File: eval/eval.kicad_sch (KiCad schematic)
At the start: 10 parts, among them J1 TC2030, U1 STM32G0B1CBTx

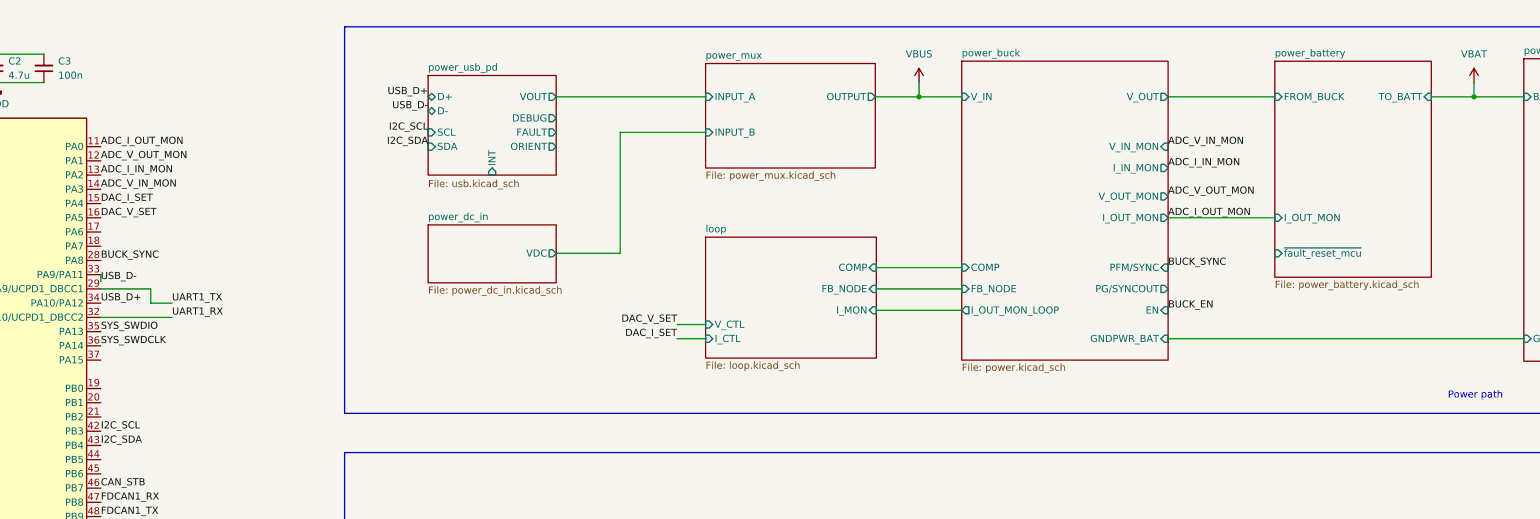
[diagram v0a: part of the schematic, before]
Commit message: [sch] Remote volt-drop detect and NAND latch
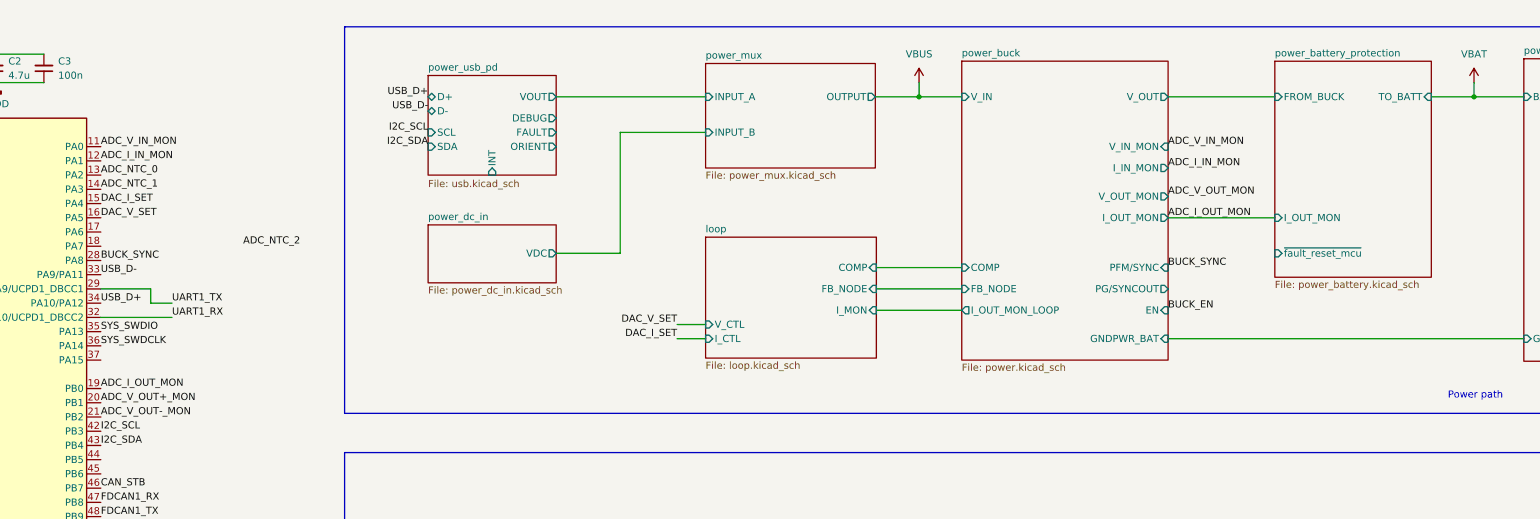
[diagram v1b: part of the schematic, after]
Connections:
- net ADC_I_IN_MON: now also U1.12 (PA1); no longer U1.13 (PA2)
- net ADC_I_OUT_MON: now also U1.19 (PB0); no longer U1.11 (PA0)
- net ADC_V_IN_MON: now also U1.11 (PA0); no longer U1.14 (PA3)
- net ADC_V_OUT_MON: no longer U1.12 (PA1)
- net ADC_V_OUT+_MON: now reaches U1.20 (PB1)
- net ADC_V_OUT-_MON: now reaches U1.21 (PB2)
- new net ADC_NTC_0: U1.13 (PA2)
- new net ADC_NTC_1: U1.14 (PA3)
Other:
- sheet power_battery renamed power_battery_protection
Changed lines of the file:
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@@
 	(wire
 		(pts
-			(xy 107.95 83.82) (xy 107.95 82.55)
-		)
-		(stroke
-			(width 0)
-			(type default)
-		)
-	)
-	(wire
-		(pts
 			(xy 107.95 85.09) (xy 116.84 85.09)
 		)
@@
 	)
 	(label "ADC_I_IN_MON"
+		(at 107.95 62.23 0)
+		(effects
+			(font
+				(size 1.27 1.27)
+			)
+			(justify left bottom)
+		)
+	)
+	(label "ADC_NTC_2"
+		(at 133.35 77.47 0)
+		(effects
+			(font
+				(size 1.27 1.27)
+			)
+			(justify left bottom)
+		)
+	)
+	(label "ADC_I_IN_MON"
 		(at 298.45 63.5 0)
 		(effects
@@
 		)
 	)
-	(label "ADC_I_OUT_MON"
+	(label "ADC_V_IN_MON"
 		(at 107.95 59.69 0)
 		(effects
@@
 		)
 	)
-	(label "ADC_I_IN_MON"
-		(at 107.95 64.77 0)
-		(effects
-			(font
-				(size 1.27 1.27)
-			)
-			(justify left bottom)
-		)
-	)
 	(label "ADC_V_OUT_MON"
 		(at 298.45 68.58 0)
@@
 		)
 	)
+	(label "ADC_I_OUT_MON"
+		(at 107.95 102.87 0)
+		(effects
+			(font
+				(size 1.27 1.27)
+			)
+			(justify left bottom)
+		)
+	)
 	(label "SYS_SWDCLK"
 		(at 63.5 195.58 0)
@@
 		)
 	)
-	(label "ADC_V_OUT_MON"
-		(at 107.95 62.23 0)
+	(label "ADC_V_OUT-_MON"
+		(at 107.95 107.95 0)
+		(effects
+			(font
+				(size 1.27 1.27)
+			)
+			(justify left bottom)
+		)
+	)
+	(label "ADC_NTC_1"
+		(at 107.95 67.31 0)
 		(effects
 			(font
@@
 	)
 	(label "USB_D-"
-		(at 107.95 83.82 0)
+		(at 107.95 82.55 0)
 		(effects
 			(font
@@
 		)
 	)
-	(label "ADC_V_IN_MON"
-		(at 107.95 67.31 0)
+	(label "FDCAN1_RX"
+		(at 107.95 123.19 0)
 		(effects
 			(font
@@
 		)
 	)
-	(label "FDCAN1_RX"
-		(at 107.95 123.19 0)
+	(label "LCD_CS"
+		(at 107.95 133.35 0)
 		(effects
 			(font
@@
 		)
 	)
-	(label "LCD_CS"
-		(at 107.95 133.35 0)
+	(label "ADC_NTC_0"
+		(at 107.95 64.77 0)
 		(effects
 			(font
@@
 		)
 	)
+	(label "ADC_V_OUT+_MON"
+		(at 107.95 105.41 0)
+		(effects
+			(font
+				(size 1.27 1.27)
+			)
+			(justify left bottom)
+		)
+	)
 	(symbol
 		(lib_id "power:GNDA")
@@
 			(color 0 0 0 0)
 		)
-		(property "Sheetname" "power_battery"
+		(property "Sheetname" "power_battery_protection"
 			(at 317.5 43.7384 0)
 			(show_name no)

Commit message: [sch] Use a 74lvc1 as oring of alart
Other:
- sheet power_battery_protection ports: added MCU_EN, NEG_V_ALARM, OVER_I_ALARM; removed ~{fault_reset_mcu}
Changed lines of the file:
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@@
-			)
-		)
-		(pin "~{fault_reset_mcu}" input
-			(at 317.5 78.74 180)
-			(effects
-				(font
-					(size 1.27 1.27)
-				)
-				(justify left)
 			)
 		)
@@
 			(effects
 				(font
+					(size 1.27 1.27)
+				)
+				(justify right)
+			)
+		)
+		(pin "MCU_EN" input
+			(at 345.44 59.69 0)
+			(effects
+				(font
+					(size 1.27 1.27)
+				)
+				(justify right)
+			)
+		)
+		(pin "NEG_V_ALARM" input
+			(at 345.44 63.5 0)
+			(effects
+				(font
+					(size 1.27 1.27)
+				)
+				(justify right)
+			)
+		)
+		(pin "OVER_I_ALARM" input
+			(at 345.44 67.31 0)
+			(effects
+				(font

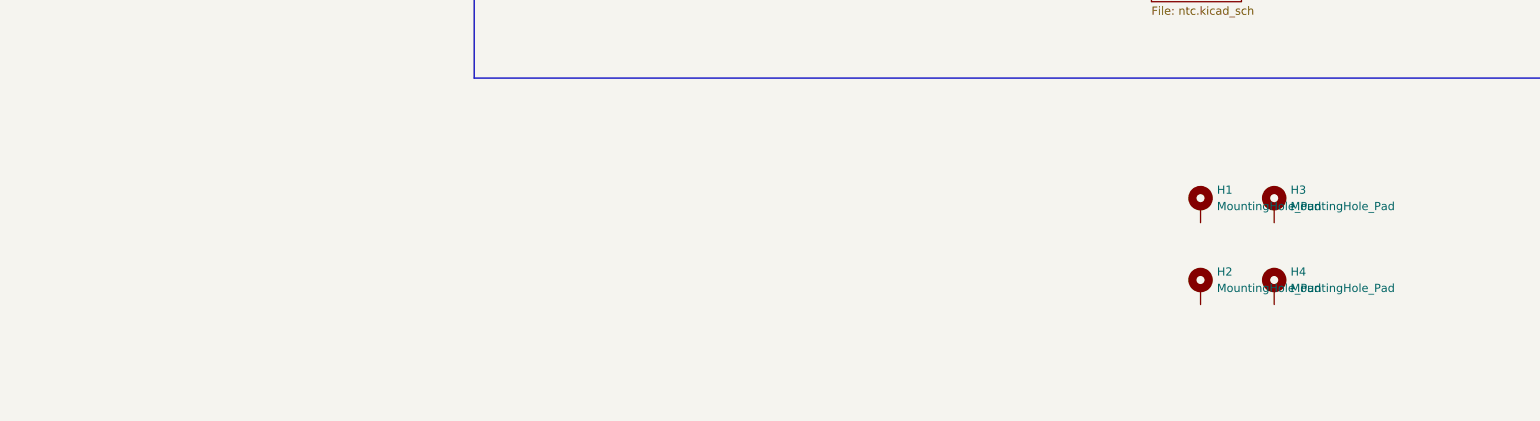
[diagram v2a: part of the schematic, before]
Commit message: [sch] Remove RC delay, add 74lvc trigger
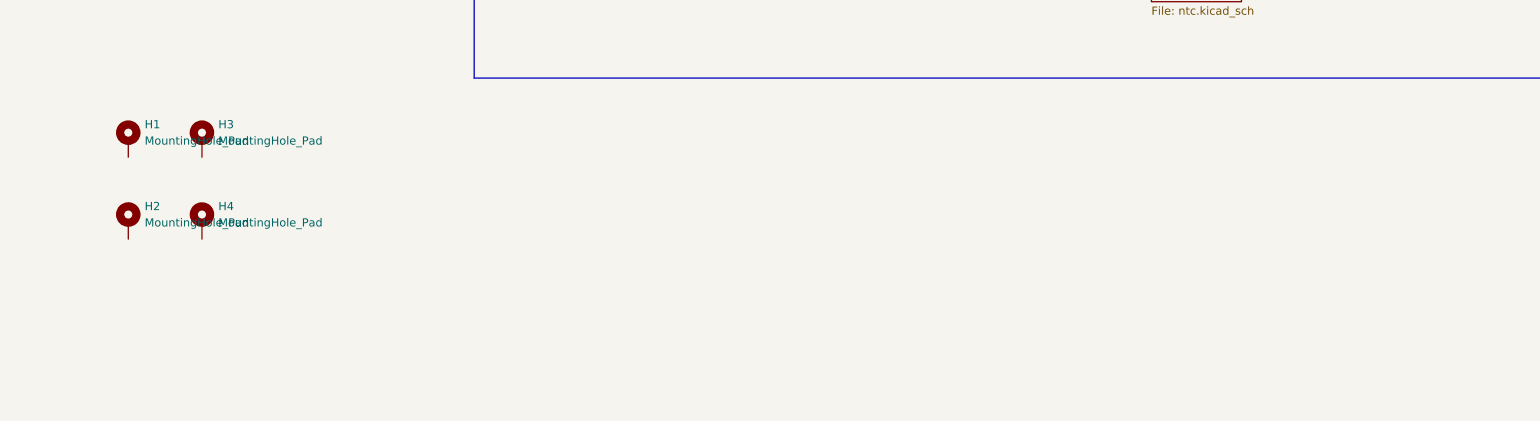
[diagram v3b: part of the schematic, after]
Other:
- moved on the sheet: H1, H2, H3, H4
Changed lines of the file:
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@@
 	(symbol
 		(lib_id "Mechanical:MountingHole_Pad")
-		(at 264.16 203.2 0)
+		(at 97.79 193.04 0)
 		(unit 1)
 		(body_style 1)
@@
 		(fields_autoplaced yes)
 		(property "Reference" "H1"
-			(at 266.7 200.6599 0)
+			(at 100.33 190.4999 0)
 			(show_name no)
 			(do_not_autoplace no)
@@
 		)
 		(property "Value" "MountingHole_Pad"
-			(at 266.7 203.1999 0)
+			(at 100.33 193.0399 0)
 			(show_name no)
 			(do_not_autoplace no)
@@
 		)
 		(property "Footprint" "MountingHole:MountingHole_2.2mm_M2_Pad_Via"
-			(at 264.16 203.2 0)
+			(at 97.79 193.04 0)
 			(hide yes)
 			(show_name no)
@@
 		)
 		(property "Datasheet" ""
-			(at 264.16 203.2 0)
+			(at 97.79 193.04 0)
 			(hide yes)
 			(show_name no)
@@
 		)
 		(property "Description" "Mounting Hole with connection"
-			(at 264.16 203.2 0)
+			(at 97.79 193.04 0)
 			(hide yes)
 			(show_name no)
@@
 	(symbol
 		(lib_id "Mechanical:MountingHole_Pad")
-		(at 264.16 215.9 0)
+		(at 97.79 205.74 0)
 		(unit 1)
 		(body_style 1)
@@
 		(fields_autoplaced yes)
 		(property "Reference" "H2"
-			(at 266.7 213.3599 0)
+			(at 100.33 203.1999 0)
 			(show_name no)
 			(do_not_autoplace no)
@@
 		)
 		(property "Value" "MountingHole_Pad"
-			(at 266.7 215.8999 0)
+			(at 100.33 205.7399 0)
 			(show_name no)
 			(do_not_autoplace no)
@@
 		)
 		(property "Footprint" "MountingHole:MountingHole_2.2mm_M2_Pad_Via"
-			(at 264.16 215.9 0)
+			(at 97.79 205.74 0)
 			(hide yes)
 			(show_name no)
@@
 		)
 		(property "Datasheet" ""
-			(at 264.16 215.9 0)
+			(at 97.79 205.74 0)
 			(hide yes)
 			(show_name no)
@@
 		)
 		(property "Description" "Mounting Hole with connection"
-			(at 264.16 215.9 0)
+			(at 97.79 205.74 0)
 			(hide yes)
 			(show_name no)
@@
 	(symbol
 		(lib_id "Mechanical:MountingHole_Pad")
-		(at 275.59 203.2 0)
+		(at 109.22 193.04 0)
 		(unit 1)
 		(body_style 1)
@@
 		(fields_autoplaced yes)
 		(property "Reference" "H3"
-			(at 278.13 200.6599 0)
+			(at 111.76 190.4999 0)
 			(show_name no)
 			(do_not_autoplace no)
@@
 		)
 		(property "Value" "MountingHole_Pad"
-			(at 278.13 203.1999 0)
+			(at 111.76 193.0399 0)
 			(show_name no)
 			(do_not_autoplace no)
@@
 		)
 		(property "Footprint" "MountingHole:MountingHole_2.2mm_M2_Pad_Via"
-			(at 275.59 203.2 0)
+			(at 109.22 193.04 0)
 			(hide yes)
 			(show_name no)
@@
 		)
 		(property "Datasheet" ""
-			(at 275.59 203.2 0)
+			(at 109.22 193.04 0)
 			(hide yes)
 			(show_name no)
@@
 		)
 		(property "Description" "Mounting Hole with connection"
-			(at 275.59 203.2 0)
+			(at 109.22 193.04 0)
 			(hide yes)
 			(show_name no)
@@
 	(symbol
 		(lib_id "Mechanical:MountingHole_Pad")
-		(at 275.59 215.9 0)
+		(at 109.22 205.74 0)
 		(unit 1)
 		(body_style 1)
@@
 		(fields_autoplaced yes)
 		(property "Reference" "H4"
-			(at 278.13 213.3599 0)
+			(at 111.76 203.1999 0)
 			(show_name no)
 			(do_not_autoplace no)
@@
 		)
 		(property "Value" "MountingHole_Pad"
-			(at 278.13 215.8999 0)
+			(at 111.76 205.7399 0)
 			(show_name no)
 			(do_not_autoplace no)
@@
 		)
 		(property "Footprint" "MountingHole:MountingHole_2.2mm_M2_Pad_Via"
-			(at 275.59 215.9 0)
+			(at 109.22 205.74 0)
 			(hide yes)
 			(show_name no)
@@
 		)
 		(property "Datasheet" ""
-			(at 275.59 215.9 0)
+			(at 109.22 205.74 0)
 			(hide yes)
 			(show_name no)
@@
 		)
 		(property "Description" "Mounting Hole with connection"
-			(at 275.59 215.9 0)
-			(hide yes)
-			(show_name no)
+			(at 109.22 205.74 0)
+			(hide yes)
+			(show_name no)
